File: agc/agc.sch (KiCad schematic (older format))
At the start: 120 parts, among them J1 SMA_DAC, J2 SMA_LPTR, J3 SMA_DRIVER, J4 SMA_RX, J5 SIL10, K1 TR, K2 CONN_3, K3 VIN, K4 CONN_3, K5 TR, K7 HVMON, P1 COUPLED_TEST, P10 CONN_2, P2 FWD_FAULT, P3 REF_FAULT, P4 CONN_8X2, P5 COUPLED_TEST, P6 TP_VCC, P7 COUPLED_TEST, P8 COUPLED_TEST, P9 COUPLED_TEST, U1 BA08CC0WFP, U10 74AHC1G04, U11 74AHC1G04, U12 78SRH-5/2-C, U2 HMC475, U3 HMC595, U4 HMC595, U5 HMC595, U6 74AHC1G04, U7 ISL3281E, U8 MGA-61563, U9 LTC2914-2

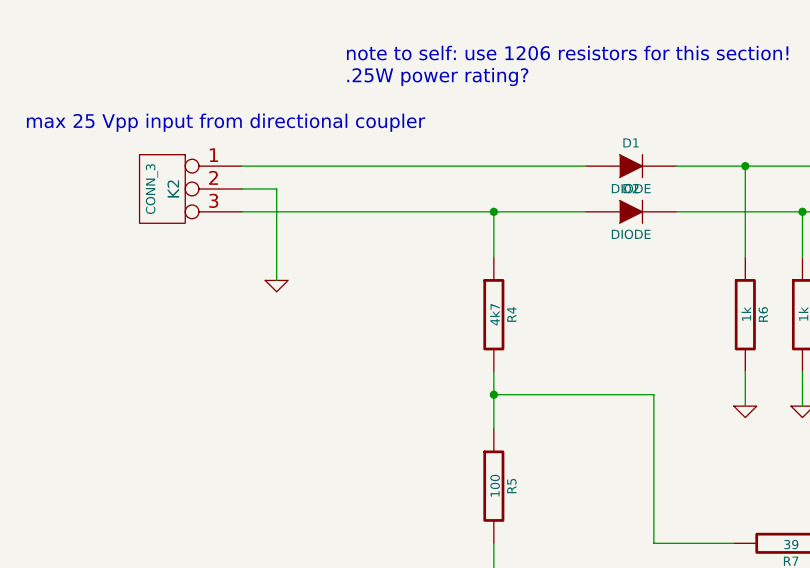
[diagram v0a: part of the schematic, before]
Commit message: picked tx hptr diode bias with higher linearity, added missing resistors for coupler in control board
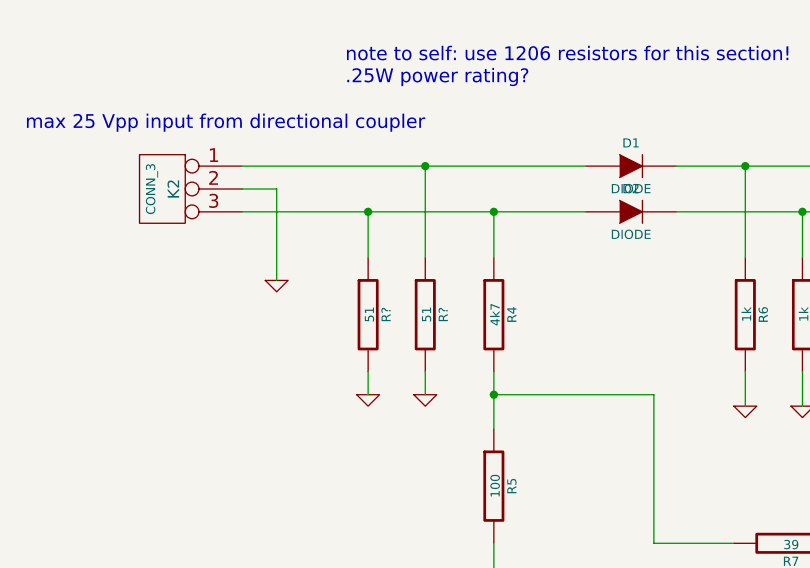
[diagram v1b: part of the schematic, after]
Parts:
- added R? (x2): 51, SMD_Packages:SM1206, symbol R
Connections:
- net GND: now also R?.2, R?.2
- net at D2.1 (A), K2.3 (P3), R4.1: now also R?.1
- net at D1.1 (A), K2.1 (P1): now also R?.1
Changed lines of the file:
@@
 Wire Wire Line
 	15300 13700 15650 13700
+$Comp
+L R R?
+U 1 1 53CEDEDC
+P 2900 3100
+F 0 "R?" V 2980 3100 40  0000 C CNN
+F 1 "51" V 2907 3101 40  0000 C CNN
+F 2 "SMD_Packages:SM1206" V 2830 3100 30  0001 C CNN
+F 3 "" H 2900 3100 30  0000 C CNN
+	1    2900 3100
+	1    0    0    -1
+$EndComp
+$Comp
+L R R?
+U 1 1 53CEDEE7
+P 2650 3100
+F 0 "R?" V 2730 3100 40  0000 C CNN
+F 1 "51" V 2657 3101 40  0000 C CNN
+F 2 "SMD_Packages:SM1206" V 2580 3100 30  0001 C CNN
+F 3 "" H 2650 3100 30  0000 C CNN
+	1    2650 3100
+	1    0    0    -1
+$EndComp
+$Comp
+L GND #PWR?
+U 1 1 53CEDEF2
+P 2650 3450
+F 0 "#PWR?" H 2650 3450 30  0001 C CNN
+F 1 "GND" H 2650 3380 30  0001 C CNN
+F 2 "" H 2650 3450 60  0000 C CNN
+F 3 "" H 2650 3450 60  0000 C CNN
+	1    2650 3450
+	1    0    0    -1
+$EndComp
+$Comp
+L GND #PWR?
+U 1 1 53CEDEFD
+P 2900 3450
+F 0 "#PWR?" H 2900 3450 30  0001 C CNN
+F 1 "GND" H 2900 3380 30  0001 C CNN
+F 2 "" H 2900 3450 60  0000 C CNN
+F 3 "" H 2900 3450 60  0000 C CNN
+	1    2900 3450
+	1    0    0    -1
+$EndComp
+Wire Wire Line
+	2900 2850 2900 2450
+Connection ~ 2900 2450
+Wire Wire Line
+	2650 2650 2650 2850
+Connection ~ 2650 2650
+Wire Wire Line
+	2650 3350 2650 3450
+Wire Wire Line
+	2900 3350 2900 3450
 $EndSCHEMATC

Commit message: moved agc coupled signal splitting off-board
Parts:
- removed D1, D2: DIODE, Diodes_SMD:Diode-SMB_Handsoldering, symbol DIODE
- removed K2, K4: CONN_3, Connect:PINHEAD1-3, symbol CONN_3
- removed P1: COUPLED_TEST, Connect:PINTST, symbol CONN_1
- removed R10, R7: 39, SMD_Packages:SM1206, symbol R
- removed R17, R21: DNP, SMD_Packages:SM0805, symbol R
- removed R4: 4k7, SMD_Packages:SM1206, symbol R
- removed R5: 100, SMD_Packages:SM1206, symbol R
- removed R6, R8: 1k, SMD_Packages:SM1206, symbol R
- removed R9: 10, SMD_Packages:SM1206, symbol R
- removed R? (x2): 51, SMD_Packages:SM1206, symbol R
- added J6: SMA_LPTR, sma:sma, symbol SMA
- added U14, U15, U16: SMP1330-005LF, SMD_Packages:SOT23, symbol SMP1330-005LF
- J5: footprint (none) -> Connect:SIL-10
- P10: footprint (none) -> Connect:PINHEAD1-2
- P4: footprint (none) -> Connect:VASCH8x2
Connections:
- net GND: now also J6.2 (GND), J6.3 (GND), J6.4 (GND), J6.5 (GND), U14.1 (GND), U14.2 (GND), U15.1 (GND), U15.2 (GND), U16.1 (GND), U16.2 (GND)
- net at C11.2, J2.1 (RF): now also U14.3 (LIM)
- net at J4.1 (RF), R27.1, R32.2: now also U16.3 (LIM)
- net at R11.2, R13.1: now also J6.1 (RF)
- net at C12.1, R13.2, R14.2: now also U15.3 (LIM)
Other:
- note added: "pi network for\npossible filter/attenuator"
- note removed: "T network for\nattenuator\n"
- note removed: "max 25 Vpp input from directional coupler"
- note removed: "note to self: use 1206 resistors for this section!\n.25W power rating?"

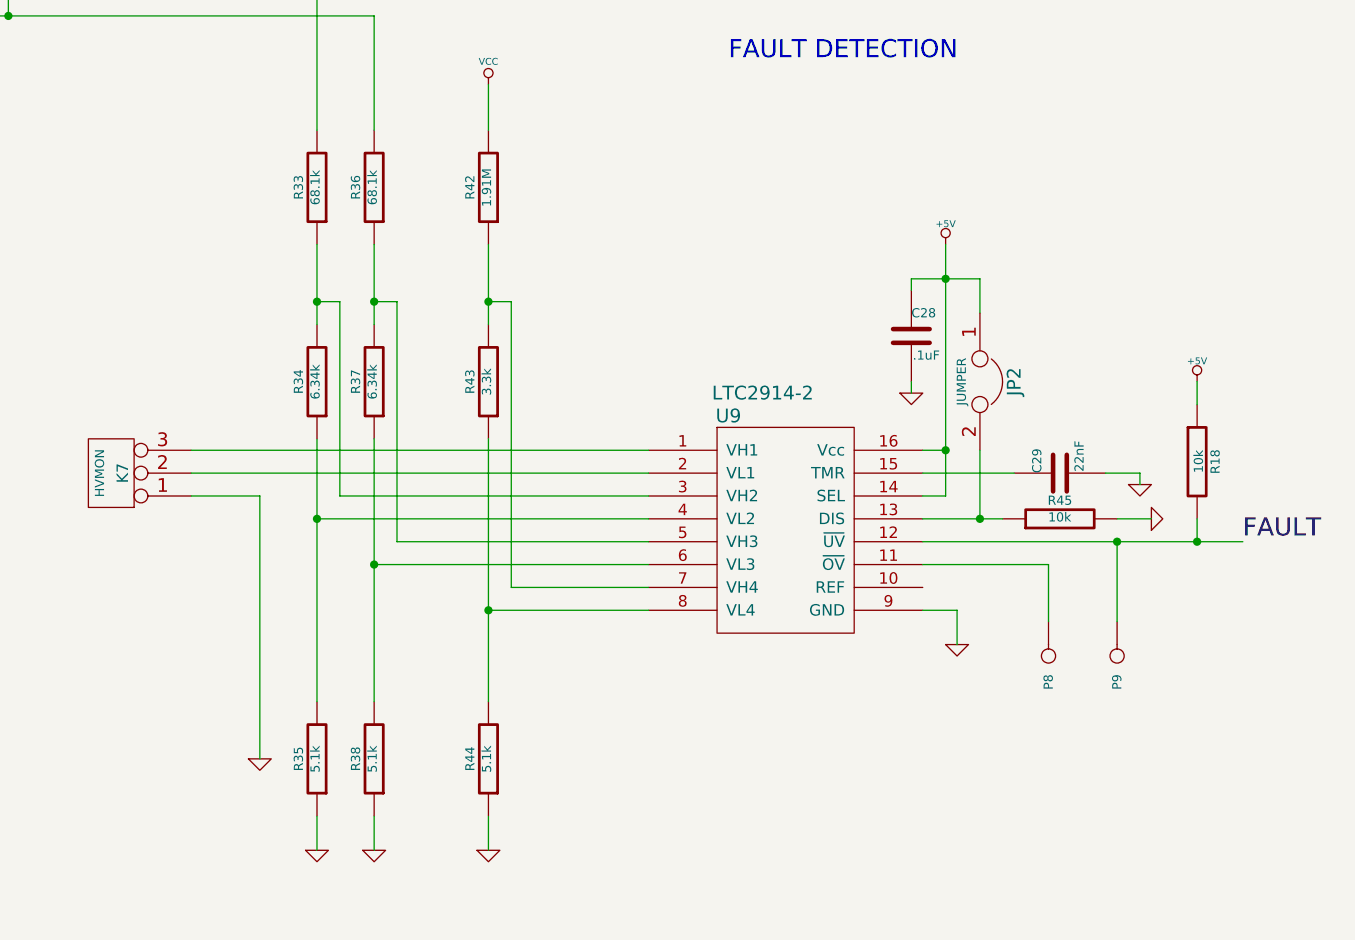
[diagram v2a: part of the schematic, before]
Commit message: added limiters to agc
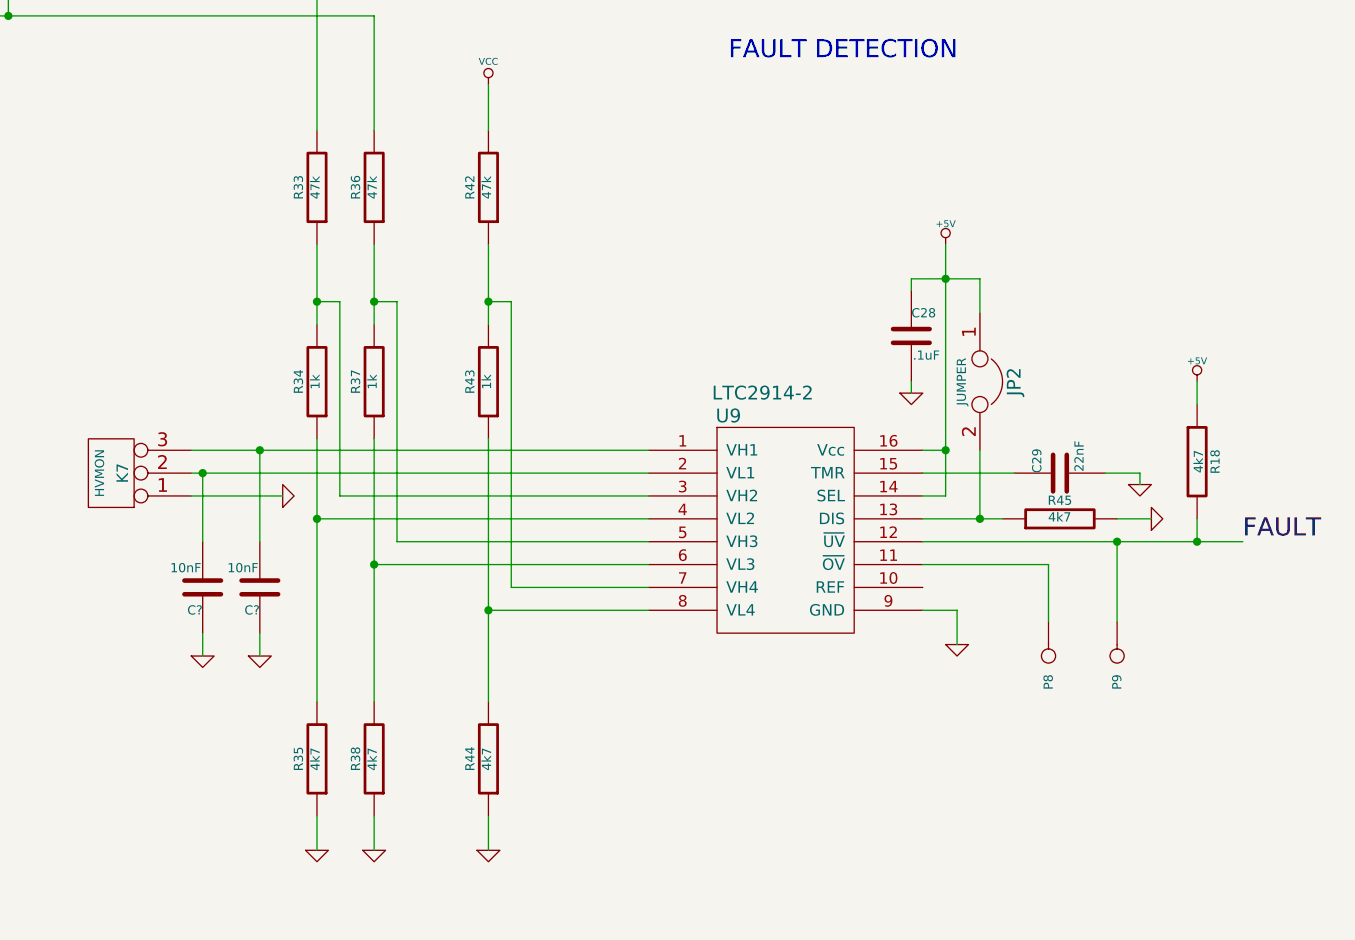
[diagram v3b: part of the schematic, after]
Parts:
- added C? (x2): 10nF, SMD_Packages:SM0805, symbol C
- R18, R45: value 10k -> 4k7
- R33, R36: value 68.1k -> 47k
- R34, R37: value 6.34k -> 1k
- R35, R38, R44: value 5.1k -> 4k7
- R42: value 1.91M -> 47k
- R43: value 3.3k -> 1k
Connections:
- net GND: now also C?.1, C?.1
- net at K7.3 (P3), U9.1 (VH1): now also C?.2
- net at K7.2 (PM), U9.2 (VL1): now also C?.2
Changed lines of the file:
@@
 P 16850 9000
 F 0 "R33" V 16930 9000 40  0000 C CNN
-F 1 "68.1k" V 16857 9001 40  0000 C CNN
+F 1 "47k" V 16857 9001 40  0000 C CNN
 F 2 "SMD_Packages:SM0805" V 16780 9000 30  0001 C CNN
 F 3 "" H 16850 9000 30  0000 C CNN
@@
 P 16850 11500
 F 0 "R35" V 16930 11500 40  0000 C CNN
-F 1 "5.1k" V 16857 11501 40  0000 C CNN
+F 1 "4k7" V 16857 11501 40  0000 C CNN
 F 2 "SMD_Packages:SM0805" V 16780 11500 30  0001 C CNN
 F 3 "" H 16850 11500 30  0000 C CNN
@@
 P 16850 9850
 F 0 "R34" V 16930 9850 40  0000 C CNN
-F 1 "6.34k" V 16857 9851 40  0000 C CNN
+F 1 "1k" V 16857 9851 40  0000 C CNN
 F 2 "SMD_Packages:SM0805" V 16780 9850 30  0001 C CNN
 F 3 "" H 16850 9850 30  0000 C CNN
@@
 P 17100 9000
 F 0 "R36" V 17180 9000 40  0000 C CNN
-F 1 "68.1k" V 17107 9001 40  0000 C CNN
+F 1 "47k" V 17107 9001 40  0000 C CNN
 F 2 "SMD_Packages:SM0805" V 17030 9000 30  0001 C CNN
 F 3 "" H 17100 9000 30  0000 C CNN
@@
 P 17100 11500
 F 0 "R38" V 17180 11500 40  0000 C CNN
-F 1 "5.1k" V 17107 11501 40  0000 C CNN
+F 1 "4k7" V 17107 11501 40  0000 C CNN
 F 2 "SMD_Packages:SM0805" V 17030 11500 30  0001 C CNN
 F 3 "" H 17100 11500 30  0000 C CNN
@@
 P 17100 9850
 F 0 "R37" V 17180 9850 40  0000 C CNN
-F 1 "6.34k" V 17107 9851 40  0000 C CNN
+F 1 "1k" V 17107 9851 40  0000 C CNN
 F 2 "SMD_Packages:SM0805" V 17030 9850 30  0001 C CNN
 F 3 "" H 17100 9850 30  0000 C CNN
@@
 P 17600 9850
 F 0 "R43" V 17680 9850 40  0000 C CNN
-F 1 "3.3k" V 17607 9851 40  0000 C CNN
+F 1 "1k" V 17607 9851 40  0000 C CNN
 F 2 "SMD_Packages:SM0805" V 17530 9850 30  0001 C CNN
 F 3 "" H 17600 9850 30  0000 C CNN
@@
 P 17600 11500
 F 0 "R44" V 17680 11500 40  0000 C CNN
-F 1 "5.1k" V 17607 11501 40  0000 C CNN
+F 1 "4k7" V 17607 11501 40  0000 C CNN
 F 2 "SMD_Packages:SM0805" V 17530 11500 30  0001 C CNN
 F 3 "" H 17600 11500 30  0000 C CNN
@@
 P 17600 9000
 F 0 "R42" V 17680 9000 40  0000 C CNN
-F 1 "1.91M" V 17607 9001 40  0000 C CNN
+F 1 "47k" V 17607 9001 40  0000 C CNN
 F 2 "SMD_Packages:SM0805" V 17530 9000 30  0001 C CNN
 F 3 "" H 17600 9000 30  0000 C CNN
@@
 P 20100 10450
 F 0 "R45" V 20180 10450 40  0000 C CNN
-F 1 "10k" V 20107 10451 40  0000 C CNN
+F 1 "4k7" V 20107 10451 40  0000 C CNN
 F 2 "SMD_Packages:SM0805" V 20030 10450 30  0001 C CNN
 F 3 "" H 20100 10450 30  0000 C CNN
@@
 L GND #PWR066
 U 1 1 537FD89C
-P 16600 11500
-F 0 "#PWR066" H 16600 11500 30  0001 C CNN
-F 1 "GND" H 16600 11430 30  0001 C CNN
-F 2 "" H 16600 11500 60  0000 C CNN
-F 3 "" H 16600 11500 60  0000 C CNN
-	1    16600 11500
-	1    0    0    -1
+P 16700 10350
+F 0 "#PWR066" H 16700 10350 30  0001 C CNN
+F 1 "GND" H 16700 10280 30  0001 C CNN
+F 2 "" H 16700 10350 60  0000 C CNN
+F 3 "" H 16700 10350 60  0000 C CNN
+	1    16700 10350
+	0    -1   -1   0
 $EndComp
 $Comp
@@
 P 20700 10200
 F 0 "R18" V 20780 10200 40  0000 C CNN
-F 1 "10k" V 20707 10201 40  0000 C CNN
+F 1 "4k7" V 20707 10201 40  0000 C CNN
 F 2 "SMD_Packages:SM0805" V 20630 10200 30  0001 C CNN
 F 3 "" H 20700 10200 30  0000 C CNN
@@
 Connection ~ 3050 13450
 Wire Wire Line
-	16300 10350 16600 10350
-Wire Wire Line
-	16600 10350 16600 11500
+	16300 10350 16700 10350
 Wire Wire Line
 	18300 10650 17100 10650
@@
 Wire Wire Line
 	5250 1700 5350 1700
+$Comp
+L C C?
+U 1 1 53D18787
+P 16350 10750
+F 0 "C?" H 16350 10850 40  0000 L CNN
+F 1 "10nF" H 16356 10665 40  0000 L CNN
+F 2 "SMD_Packages:SM0805" H 16388 10600 30  0001 C CNN
+F 3 "" H 16350 10750 60  0000 C CNN
+	1    16350 10750
+	-1   0    0    1
+$EndComp
+$Comp
+L C C?
+U 1 1 53D18792
+P 16600 10750
+F 0 "C?" H 16600 10850 40  0000 L CNN
+F 1 "10nF" H 16606 10665 40  0000 L CNN
+F 2 "SMD_Packages:SM0805" H 16638 10600 30  0001 C CNN
+F 3 "" H 16600 10750 60  0000 C CNN
+	1    16600 10750
+	-1   0    0    1
+$EndComp
+Wire Wire Line
+	16350 10550 16350 10250
+Connection ~ 16350 10250
+Wire Wire Line
+	16600 10150 16600 10550
+Connection ~ 16600 10150
+$Comp
+L GND #PWR?
+U 1 1 53D18C86
+P 16350 11050
+F 0 "#PWR?" H 16350 11050 30  0001 C CNN
+F 1 "GND" H 16350 10980 30  0001 C CNN
+F 2 "" H 16350 11050 60  0000 C CNN
+F 3 "" H 16350 11050 60  0000 C CNN
+	1    16350 11050
+	1    0    0    -1
+$EndComp
+Wire Wire Line
+	16350 11050 16350 10950
+Wire Wire Line
+	16600 10950 16600 11050
+$Comp
+L GND #PWR?
+U 1 1 53D18FD7
+P 16600 11050
+F 0 "#PWR?" H 16600 11050 30  0001 C CNN
+F 1 "GND" H 16600 10980 30  0001 C CNN
+F 2 "" H 16600 11050 60  0000 C CNN
+F 3 "" H 16600 11050 60  0000 C CNN
+	1    16600 11050
+	1    0    0    -1
+$EndComp
 $EndSCHEMATC
